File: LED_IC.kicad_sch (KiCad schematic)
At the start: 29 parts, among them J1 LED connector, Q1 2N7002K, Q2 2N7002K, Q5 2N7002K, U5 PCA9685PW,118

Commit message: Schematic
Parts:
- removed C3: 100nF, PCM_JLCPCB:C_0603, symbol PCM_JLCPCB-Capacitors:0603,100nF
- removed J1: LED connector, Connector_JST:JST_XH_S4B-XH-A_1x04_P2.50mm_Horizontal, symbol Connector:Conn_01x04_Pin
- removed Q1, Q2, Q5: 2N7002K, PCM_JLCPCB:Q_SOT-23, symbol PCM_JLCPCB-Transistors:NMOS,2N7002K
- removed R12, R13, R14: 200Ω, PCM_JLCPCB:R_0603, symbol PCM_JLCPCB-Resistors:0603,200Ω
- removed R18, R19, R20: 10kΩ, PCM_JLCPCB:R_0402, symbol PCM_JLCPCB-Resistors:0402,10kΩ
- added Q25, Q26: 2N7002K, PCM_JLCPCB:Q_SOT-23, symbol PCM_JLCPCB-Transistors:NMOS,2N7002K
- added R71, R72: 10kΩ, PCM_JLCPCB:R_0402, symbol PCM_JLCPCB-Resistors:0402,10kΩ
- renumbered C31 to C5, D8 to D3, D9 to D4, R15 to R12, R16 to R13, R35 to R14, R36 to R15, R37 to R16, R38 to R17, R39 to R18, R40 to R19, R41 to R20, R42 to R21, R43 to R22, R44 to R23, R45 to R24, R46 to R25, U5 to U4
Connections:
- net +5V: now also R71.1, R72.1
- net SCL_5V: now also Q25.3 (D), R71.2
- net SDA_5V: now also Q26.3 (D), R72.2
- new net +3V3: Q25.1 (G), Q26.1 (G)
- new net Chainbus.SCL: Q25.2 (S)
- new net Chainbus.SDA: Q26.2 (S)
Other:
- note added: "3V3"
- note added: "5V"
- note added: "I2C Voltage Shifter"
- note removed: "12V"
- moved on the sheet: C5

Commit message: Schematic touchup
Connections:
- net LED8: now reaches U4.15 (LED8)
- net LED9: now reaches U4.16 (LED9)
- no-connect marks 8 -> 6
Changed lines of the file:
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@@
-	)
-	(no_connect
-		(at 72.39 77.47)
 	)
 	(no_connect
@@
 	(no_connect
 		(at 72.39 59.69)
-	)
-	(no_connect
-		(at 72.39 74.93)
 	)
 	(bus_entry
@@
 		)
 	)
+	(hierarchical_label "LED9"
+		(shape passive)
+		(at 72.39 74.93 0)
+		(effects
+			(font
+				(size 1.27 1.27)
+			)
+			(justify left)
+		)
+	)
 	(hierarchical_label "LED6"
 		(shape passive)
@@
 		)
 	)
+	(hierarchical_label "LED8"
+		(shape passive)
+		(at 72.39 77.47 0)
+		(effects
+			(font
+				(size 1.27 1.27)
+			)
+			(justify left)
+		)
+	)

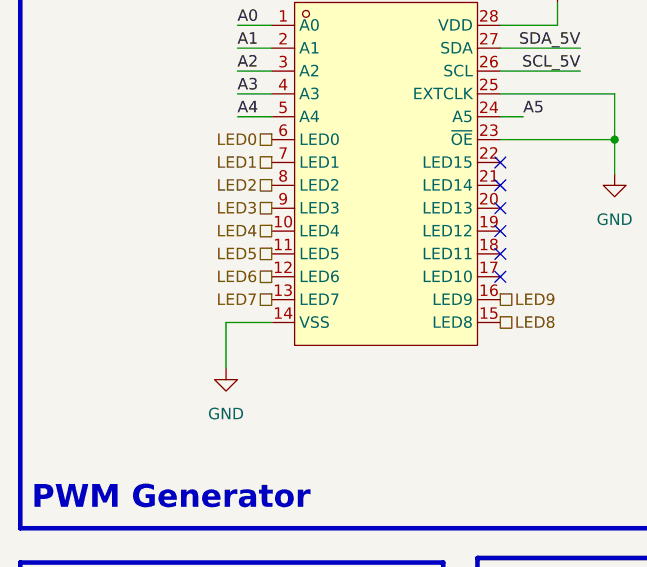
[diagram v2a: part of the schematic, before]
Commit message: PCB design
Hat allows to connect 1 LED tape at a time
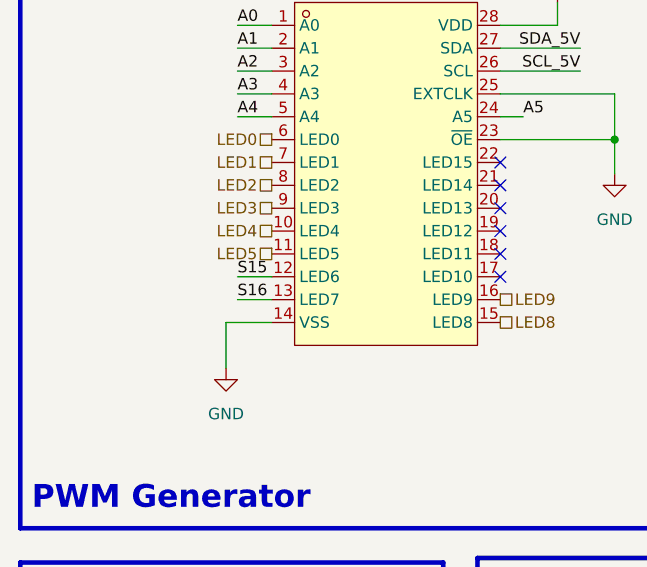
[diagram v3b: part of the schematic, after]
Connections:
- net LED6 is gone; now on net S15: U4.12 (LED6)
- net LED7 is gone; now on net S16: U4.13 (LED7)
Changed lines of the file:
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@@
+	(wire
+		(pts
+			(xy 43.18 74.93) (xy 46.99 74.93)
+		)
+		(stroke
+			(width 0)
+			(type default)
+		)
+	)
 	(wire
 		(pts
@@
 		(pts
 			(xy 78.74 41.91) (xy 78.74 44.45)
+		)
+		(stroke
+			(width 0)
+			(type default)
+		)
+	)
+	(wire
+		(pts
+			(xy 43.18 72.39) (xy 46.99 72.39)
 		)
 		(stroke
@@
 		)
 	)
+	(label "S16"
+		(at 43.18 74.93 0)
+		(effects
+			(font
+				(size 1.27 1.27)
+			)
+			(justify left bottom)
+		)
+	)
 	(label "A4"
 		(at 80.01 146.05 180)
@@
 		)
 	)
+	(label "S15"
+		(at 43.18 72.39 0)
+		(effects
+			(font
+				(size 1.27 1.27)
+			)
+			(justify left bottom)
+		)
+	)
 	(label "A2"
 		(at 43.18 49.53 0)
@@
 			)
 			(justify right bottom)
-		)
-	)
-	(hierarchical_label "LED7"
-		(shape passive)
-		(at 46.99 74.93 180)
-		(effects
-			(font
-				(size 1.27 1.27)
-			)
-			(justify right)
 		)
 	)
@@
 		)
 	)
-	(hierarchical_label "LED6"
-		(shape passive)
-		(at 46.99 72.39 180)
-		(effects
-			(font
-				(size 1.27 1.27)
-			)
-			(justify right)
-		)
-	)
